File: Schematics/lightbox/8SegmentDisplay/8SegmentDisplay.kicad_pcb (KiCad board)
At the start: 2 copper layers, 47 x 32 mm, 4 parts, among them J4 Conn_01x11_Female, U5 D148K, U6 D148K, U7 D148K

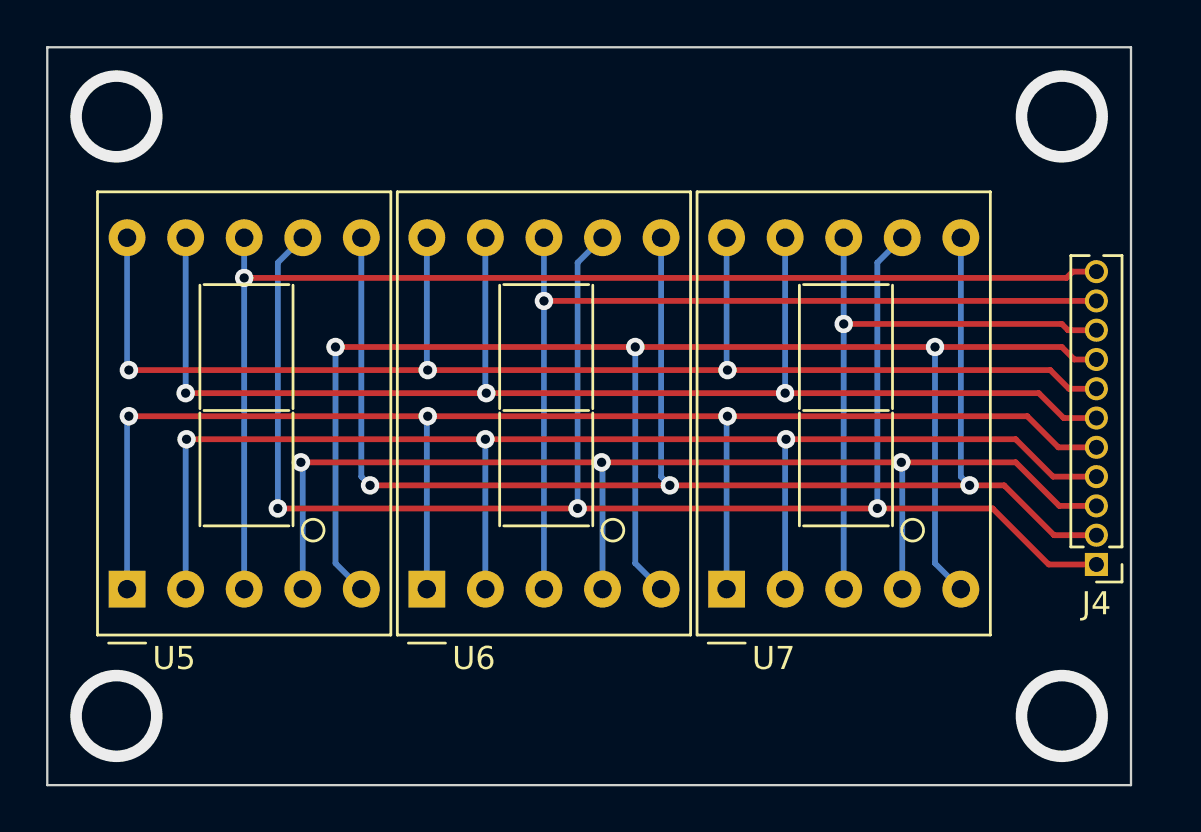
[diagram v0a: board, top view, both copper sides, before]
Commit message: Update lightbox design
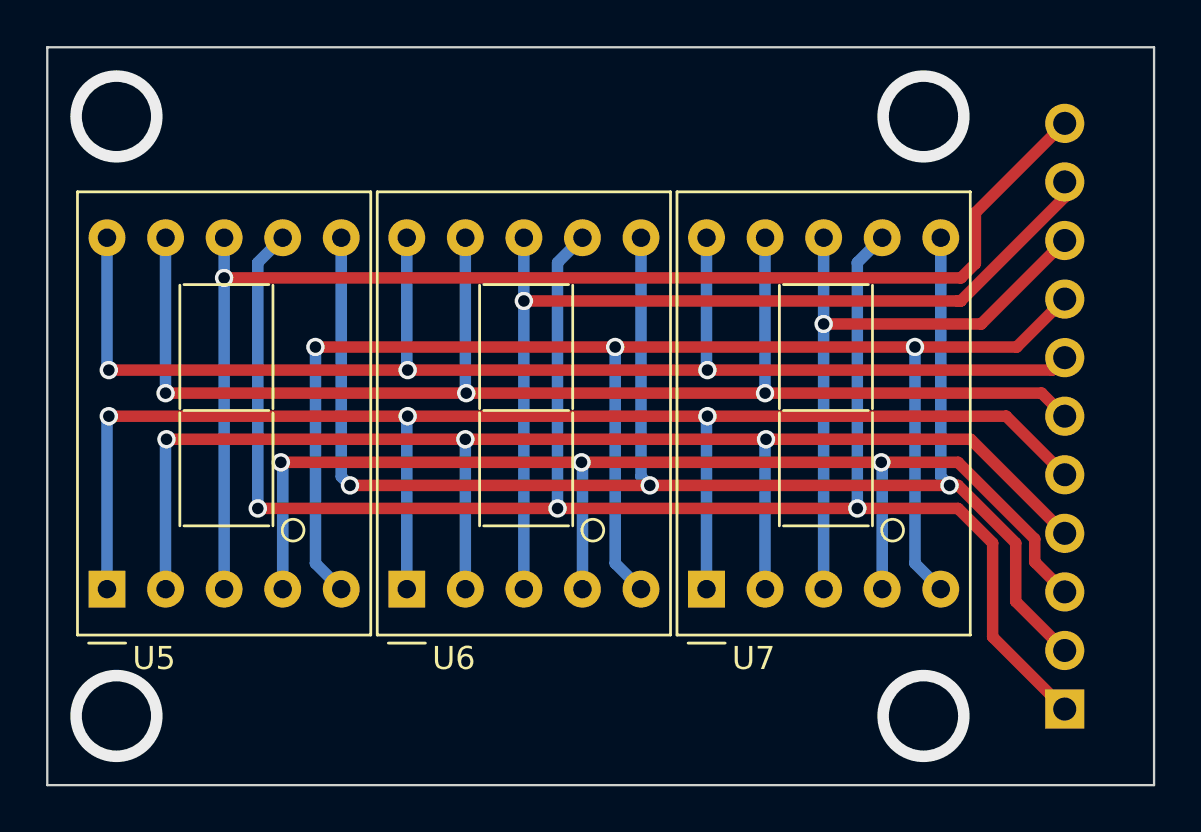
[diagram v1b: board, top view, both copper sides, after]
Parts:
- J4: footprint Connector_PinHeader_1.27mm:PinHeader_1x11_P1.27mm_Vertical -> Connector_PinHeader_2.54mm:PinHeader_1x11_P2.54mm_Horizontal; moved to B.Cu
- moved J4 6.42 mm to (156.6, 116.7), turned to 0 degrees
- moved U6 0.87 mm to (128.1, 111.5)
- moved U7 0.87 mm to (141.1, 111.5)
- moved U5 0.87 mm to (115.1, 111.5)
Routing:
- net /A: track 73.1 -> 77.5 mm
- net /Digit1: track 52.3 -> 55.8 mm
- net /B: track 65.1 -> 68.1 mm
- net /Digit2: track 39.2 -> 41.3 mm
- net /C: track 51.8 -> 53.5 mm
- net /Digit3: track 26.3 -> 27.2 mm
- net /G: track 59.6 -> 59.0 mm
- net /F: track 60.2 -> 59.6 mm
- net /D: track 59.7 -> 60.2 mm
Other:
- board size 47 x 32 mm -> 48 x 32 mm
